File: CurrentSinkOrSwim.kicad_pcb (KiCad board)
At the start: 2 copper layers, 46.5 x 58.2 mm, 23 parts, among them P101 CONN_01X02, P102 CONN_01X03, P103 CONN_01X02, P201 CONN_01X01, Q201 BUK9575, U201 LMV358, U401 LM2931D-R

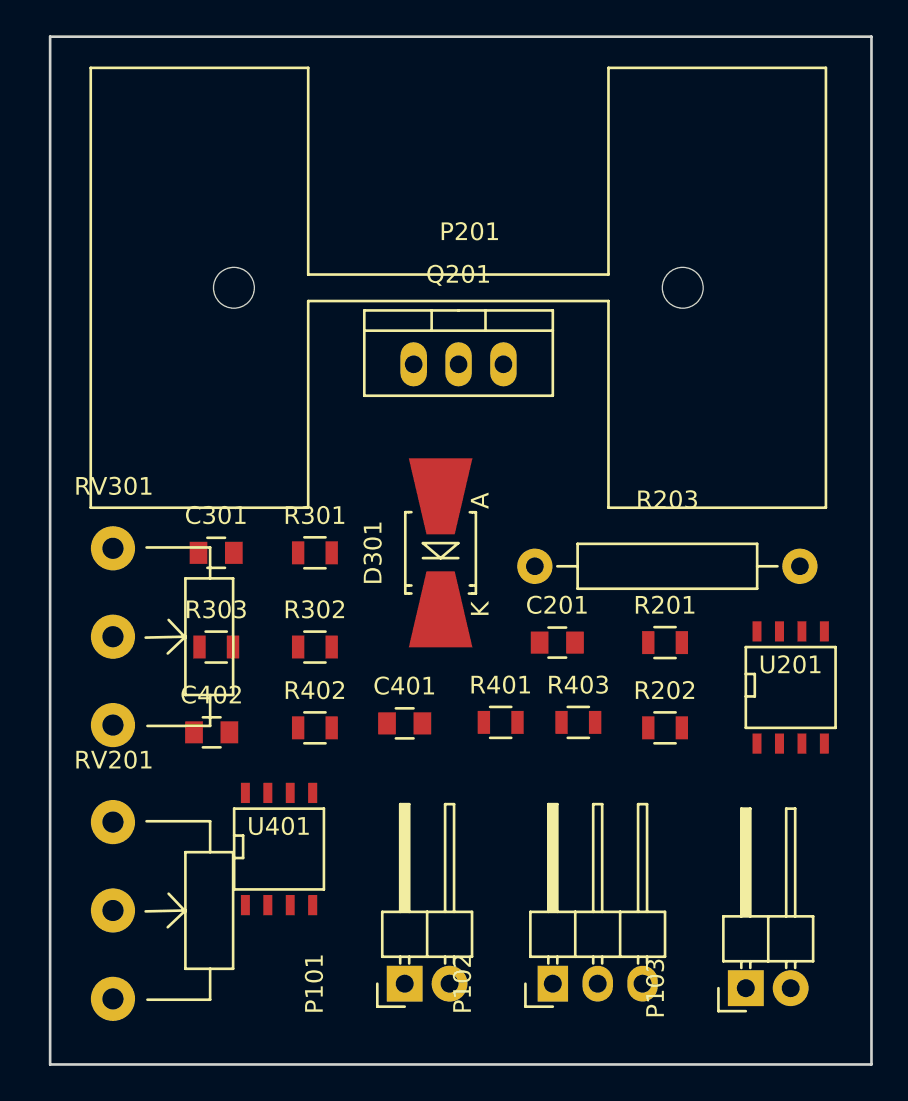
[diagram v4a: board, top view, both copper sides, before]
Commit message: Minor update to layout
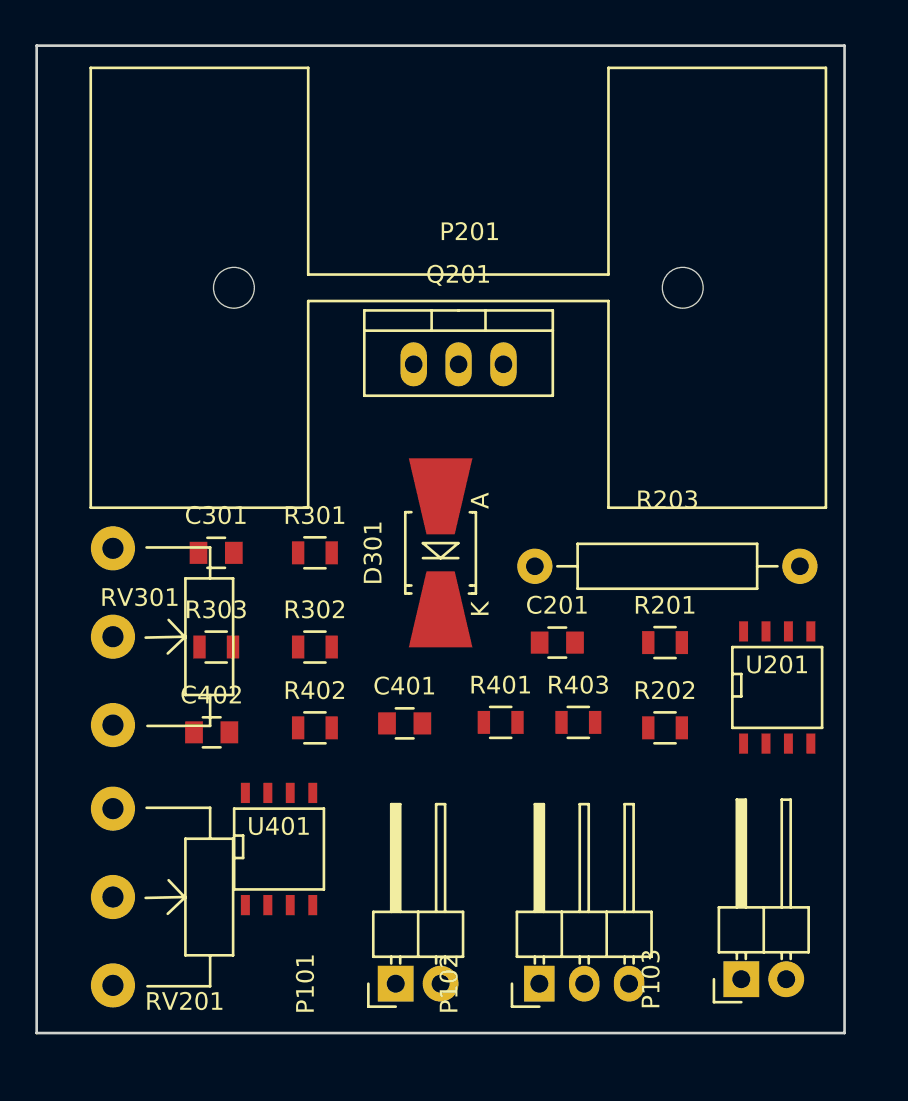
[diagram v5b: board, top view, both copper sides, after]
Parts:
- moved P102 0.76 mm to (130.0, 100.1)
- moved RV201 0.76 mm to (105.9, 90.2)
- moved U201 0.76 mm to (143.5, 83.3)
- moved P103 0.57 mm to (141.5, 99.8)
- moved P101 0.51 mm to (121.9, 100.1)
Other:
- board size 46.5 x 58.2 mm -> 45.7 x 55.9 mm
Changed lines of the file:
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@@
     (links 41)
     (no_connects 41)
-    (area 102.286999 46.406999 148.919001 148.816)
+    (area 101.524999 45.644999 148.919001 102.945001)
     (thickness 1.6)
     (drawings 4)
@@
       (effects (font (size 1 1) (thickness 0.15)))
     )
-    (fp_text value C (at 0 2.1) (layer F.Fab)
+    (fp_text value C (at 2.286 0.762) (layer F.Fab)
       (effects (font (size 1 1) (thickness 0.15)))
     )
@@
   )
   (module Pin_Headers:Pin_Header_Angled_1x02 (layer F.Cu)
-    (at 122.428 100.076 90)
+    (at 121.92 100.076 90)
     (descr "Through hole pin header")
     (tags "pin header")
@@
       (effects (font (size 1 1) (thickness 0.15)))
     )
-    (fp_text value CONN_01X02 (at 0 -3.1 90) (layer F.Fab)
+    (fp_text value CONN_01X02 (at 2.794 -2.54 90) (layer F.Fab)
       (effects (font (size 1 1) (thickness 0.15)))
     )
@@
   )
   (module Pin_Headers:Pin_Header_Angled_1x03 (layer F.Cu)
-    (at 130.81 100.076 90)
+    (at 130.048 100.076 90)
     (descr "Through hole pin header")
     (tags "pin header")
@@
       (effects (font (size 1 1) (thickness 0.15)))
     )
-    (fp_text value CONN_01X03 (at 0 -3.1 90) (layer F.Fab)
+    (fp_text value CONN_01X03 (at 2.794 -2.54 90) (layer F.Fab)
       (effects (font (size 1 1) (thickness 0.15)))
     )
@@
   )
   (module Pin_Headers:Pin_Header_Angled_1x02 (layer F.Cu)
-    (at 141.732 100.33 90)
+    (at 141.478 99.822 90)
     (descr "Through hole pin header")
     (tags "pin header")
@@
       (effects (font (size 1 1) (thickness 0.15)))
     )
-    (fp_text value CONN_01X02 (at 0 -3.1 90) (layer F.Fab)
+    (fp_text value CONN_01X02 (at 2.794 -2.794 90) (layer F.Fab)
       (effects (font (size 1 1) (thickness 0.15)))
     )
@@
       (effects (font (size 1 1) (thickness 0.15)))
     )
-    (fp_text value R (at 0 2.1) (layer F.Fab)
+    (fp_text value R (at 2.286 0.762) (layer F.Fab)
       (effects (font (size 1 1) (thickness 0.15)))
     )
@@
       (effects (font (size 1 1) (thickness 0.15)))
     )
-    (fp_text value .1 (at 7.5 4.0005) (layer F.Fab)
+    (fp_text value .1 (at 7.62 -2.286) (layer F.Fab)
       (effects (font (size 1 1) (thickness 0.15)))
     )
@@
   )
   (module Potentiometers:Potentiometer_WirePads_largePads (layer F.Cu)
-    (at 105.918 90.932)
+    (at 105.918 90.17)
     (descr "Potentiometer, Wire Pads only, RevA, 30 July 2010,")
     (tags "Potentiometer, Wire Pads only, RevA, 30 July 2010,")
-    (fp_text reference RV201 (at 0.0508 -3.49758) (layer F.SilkS)
-      (effects (font (size 1 1) (thickness 0.15)))
-    )
-    (fp_text value POT (at -1.34874 13.25118) (layer F.Fab)
+    (fp_text reference RV201 (at 4.064 10.922) (layer F.SilkS)
+      (effects (font (size 1 1) (thickness 0.15)))
+    )
+    (fp_text value POT (at 7.366 9.906) (layer F.Fab)
       (effects (font (size 1 1) (thickness 0.15)))
     )
@@
     (descr "Potentiometer, Wire Pads only, RevA, 30 July 2010,")
     (tags "Potentiometer, Wire Pads only, RevA, 30 July 2010,")
-    (fp_text reference RV301 (at 0.0508 -3.49758) (layer F.SilkS)
-      (effects (font (size 1 1) (thickness 0.15)))
-    )
-    (fp_text value POT (at -1.34874 13.25118) (layer F.Fab)
+    (fp_text reference RV301 (at 1.524 2.794) (layer F.SilkS)
+      (effects (font (size 1 1) (thickness 0.15)))
+    )
+    (fp_text value POT (at 2.794 12.954) (layer F.Fab)
       (effects (font (size 1 1) (thickness 0.15)))
     )
@@
   )
   (module SMD_Packages:SOIC-8-N (layer F.Cu)
-    (at 144.272 83.312)
+    (at 143.51 83.312)
     (descr "Module Narrow CMS SOJ 8 pins large")
     (tags "CMS SOJ")
@@
     (pad "" np_thru_hole circle (at 12.6873 -0.0127) (size 2.3114 2.3114) (drill 2.3114) (layers *.Cu *.Mask))
   )
-  (gr_line (start 148.844 46.482) (end 102.362 46.482) (angle 90) (layer Edge.Cuts) (width 0.15))
-  (gr_line (start 148.844 104.648) (end 148.844 46.482) (angle 90) (layer Edge.Cuts) (width 0.15))
-  (gr_line (start 102.362 104.648) (end 148.844 104.648) (angle 90) (layer Edge.Cuts) (width 0.15))
-  (gr_line (start 102.362 46.482) (end 102.362 104.648) (angle 90) (layer Edge.Cuts) (width 0.15))
+  (gr_line (start 147.32 46.99) (end 101.6 46.99) (angle 90) (layer Edge.Cuts) (width 0.15))
+  (gr_line (start 147.32 102.87) (end 147.32 46.99) (angle 90) (layer Edge.Cuts) (width 0.15))
+  (gr_line (start 101.6 102.87) (end 147.32 102.87) (angle 90) (layer Edge.Cuts) (width 0.15))
+  (gr_line (start 101.6 46.99) (end 101.6 102.87) (angle 90) (layer Edge.Cuts) (width 0.15))
 )

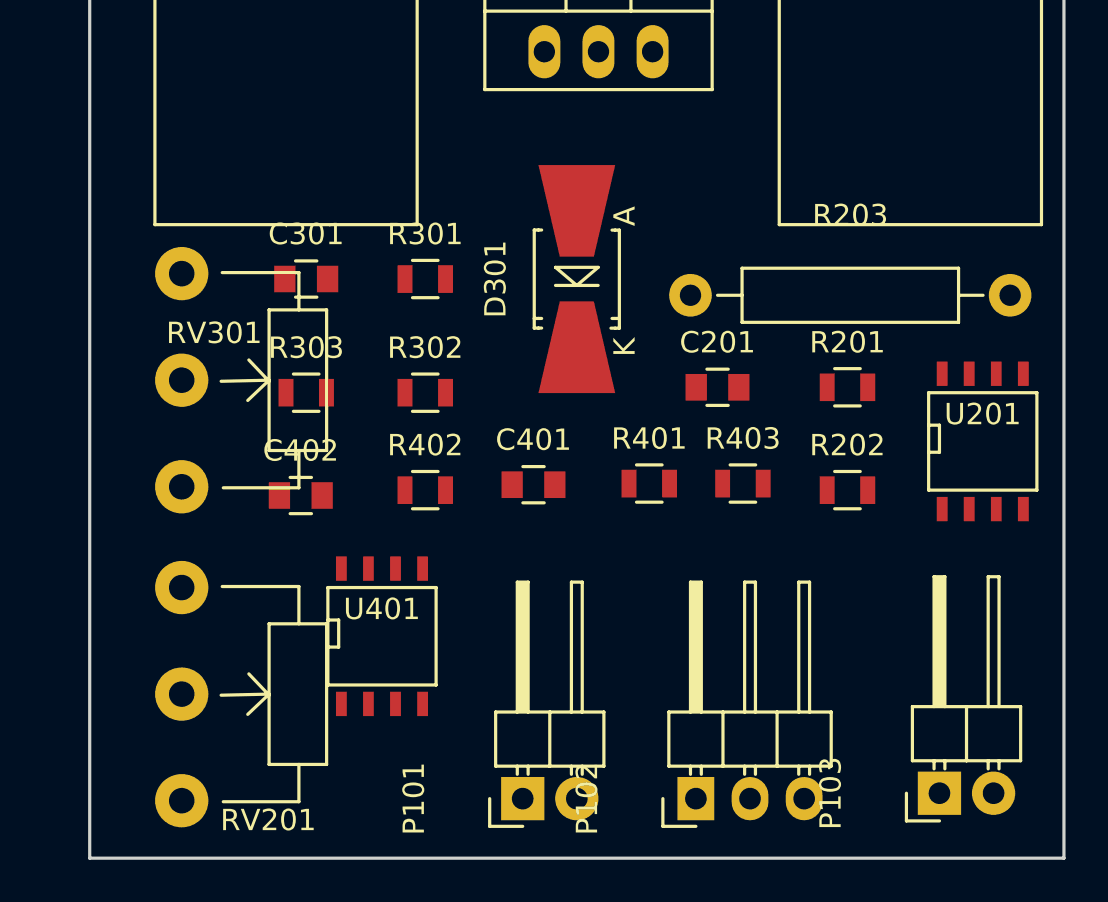
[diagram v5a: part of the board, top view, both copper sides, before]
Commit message: Add potentiometers
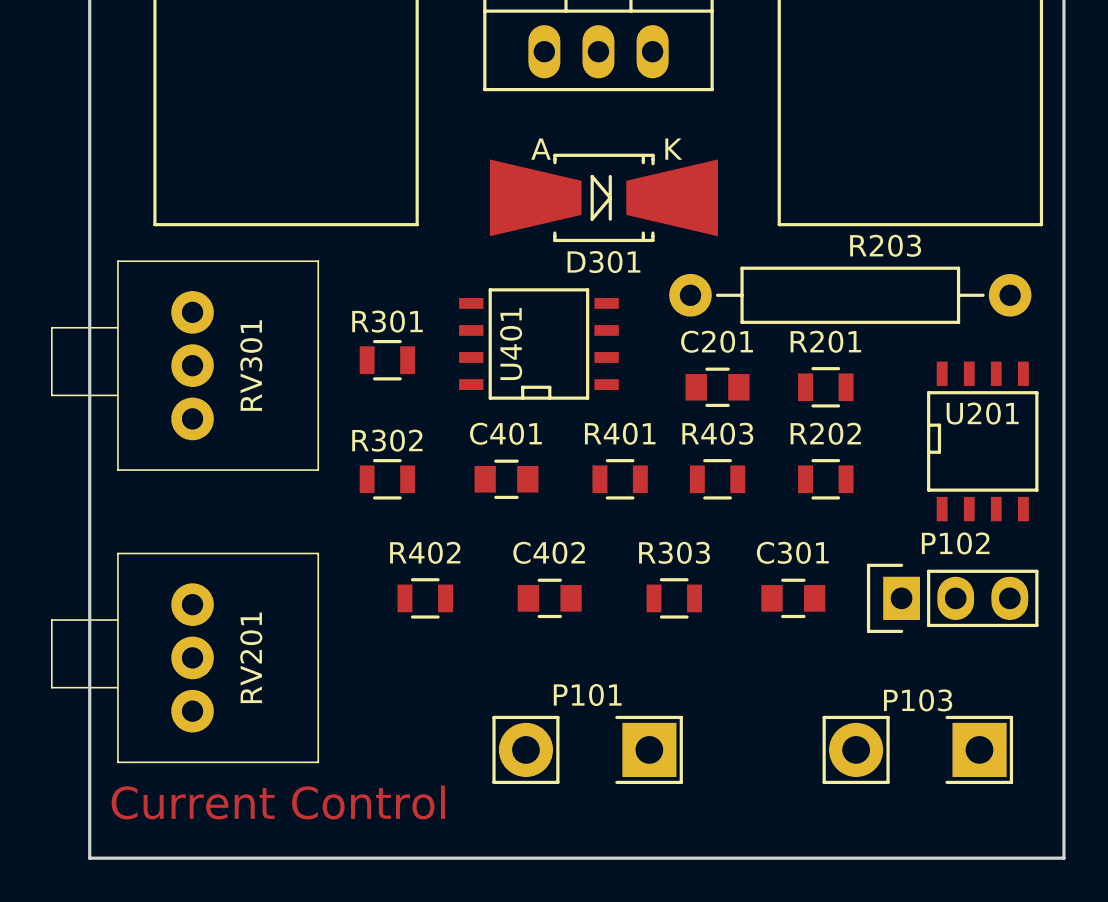
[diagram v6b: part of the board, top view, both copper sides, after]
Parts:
- P101, P103: footprint Pin_Headers:Pin_Header_Angled_1x02 -> current:Terminal_Block_200_mil
- P102: footprint Pin_Headers:Pin_Header_Angled_1x03 -> Pin_Headers:Pin_Header_Straight_1x03
- RV201, RV301: footprint Potentiometers:Potentiometer_WirePads_largePads -> current:P090L-02F25BR10K
- U401: value LM2931D-R -> LM2931
- moved C301 27.3 mm to (134.6, 90.7)
- moved R303 19.8 mm to (129.0, 90.7)
- moved U401 15.6 mm to (122.7, 78.7), turned to 90 degrees
- moved P102 13.5 mm to (139.7, 90.7)
- moved C402 12.6 mm to (123.2, 90.7)
- moved R402 5.08 mm to (117.3, 90.7)
- moved R302 4.44 mm to (115.6, 85.1)
- moved RV301 4.35 mm to (106.4, 79.8), turned to 270 degrees
- moved R301 4.20 mm to (115.6, 79.5)
- moved D301 4.02 mm to (125.7, 71.9), turned to 180 degrees
- moved P101 3.81 mm to (125.0, 97.8), turned to 180 degrees
- moved RV201 3.34 mm to (106.4, 93.5), turned to 270 degrees
- moved P103 2.27 mm to (140.5, 97.8), turned to 180 degrees
- moved R401 1.38 mm to (126.5, 85.1)
- moved C401 1.30 mm to (121.2, 85.1)
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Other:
- board text added: "Current Control"

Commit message: Update layout based on new pot and reisistor values
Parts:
- R201: value R -> 68k
- R301: value R -> 28.7k
- RV201, RV301: value POT -> 10k
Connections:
- R201 pad 1: Net-(R201-Pad1) -> 2.7V
- R201 pad 2: /Current Control/Current_Sink- -> Net-(R201-Pad2)
- R301 pad 1: Net-(R301-Pad1) -> 2.7V
- R301 pad 2: GND -> Net-(R301-Pad2)
- RV201 pad 1: Net-(RV201-Pad1) -> Net-(R201-Pad2)
- RV201 pad 2: 2.7V -> /Current Control/Current_Sink-
- RV201 pad 3: Net-(R201-Pad1) -> Net-(RV201-Pad3)
- RV301 pad 1: Net-(RV301-Pad1) -> Net-(R301-Pad2)
- RV301 pad 2: 2.7V -> GND
- RV301 pad 3: Net-(R301-Pad1) -> Net-(RV301-Pad3)
- U201 pad 3: Net-(R201-Pad1) -> Net-(R201-Pad2)
- U201 pad 5: Net-(R301-Pad1) -> Net-(R301-Pad2)

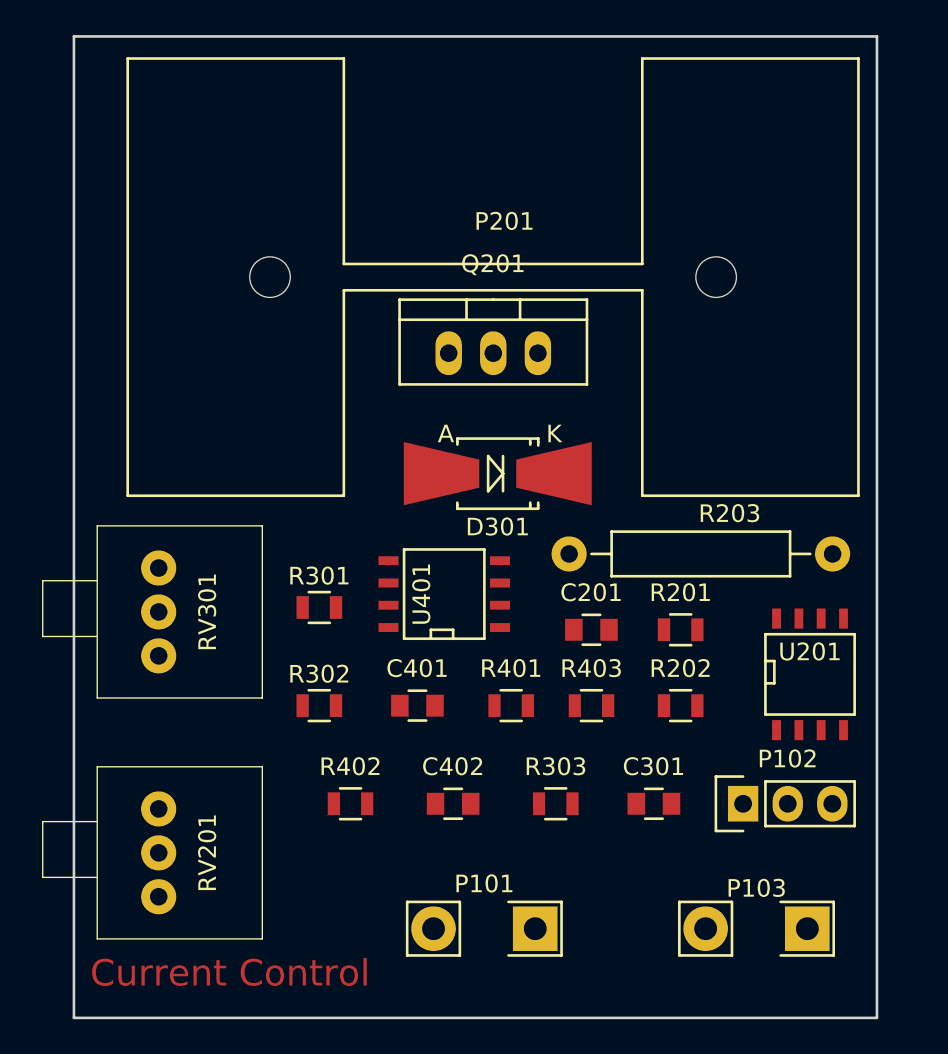
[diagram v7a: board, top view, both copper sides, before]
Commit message: Reorganization of layout, shrink board size, add ground plane
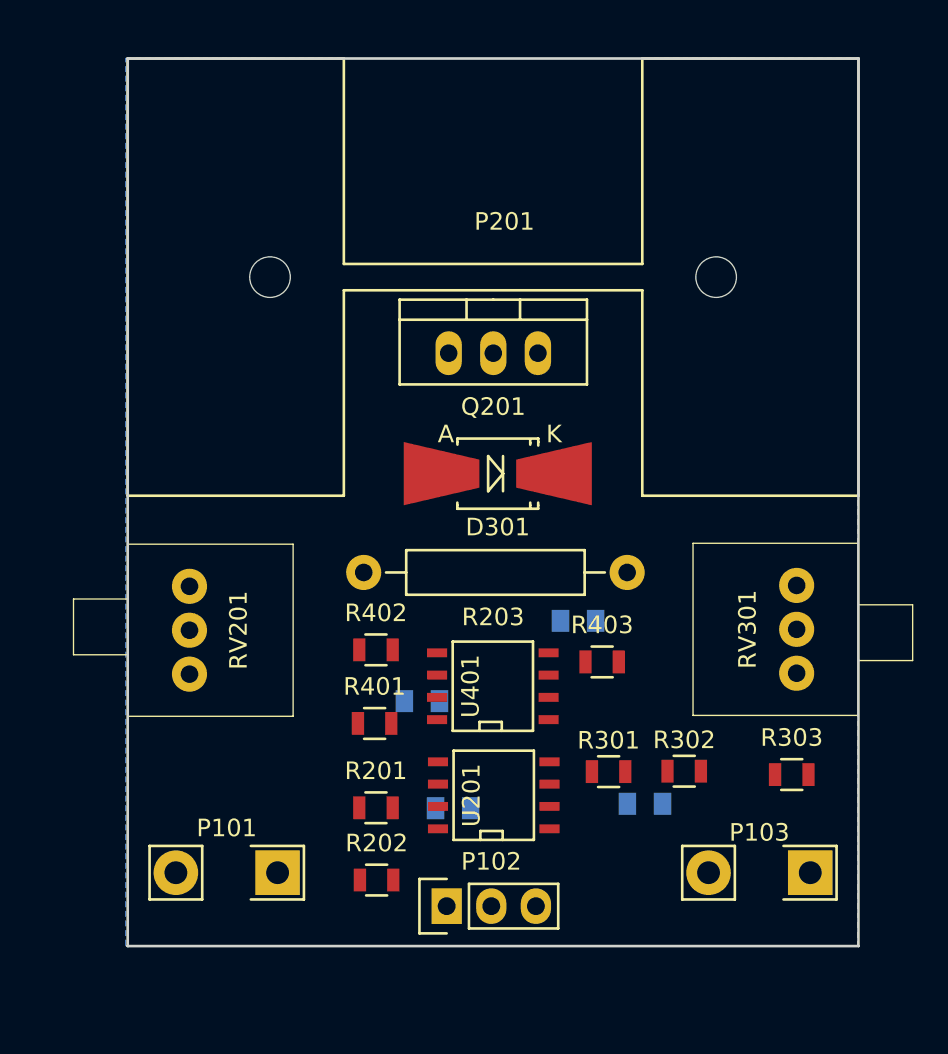
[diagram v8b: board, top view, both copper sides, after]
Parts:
- C201, C301, C401, C402: moved to B.Cu
- moved RV301 36.3 mm to (142.7, 80.7), turned to 90 degrees
- moved R302 21.1 mm to (136.3, 88.8)
- moved R201 20.1 mm to (118.8, 90.9)
- moved R202 20.0 mm to (118.8, 95.0)
- moved U201 19.3 mm to (125.5, 90.2), turned to 90 degrees
- moved R301 18.9 mm to (132.0, 88.8)
- moved P102 17.9 mm to (122.8, 96.5)
- moved P101 15.0 mm to (110.3, 94.6)
- moved R303 13.5 mm to (142.5, 89.0)
- moved RV201 12.8 mm to (108.2, 80.8)
- moved R203 11.7 mm to (118.1, 77.5)
- moved R402 8.88 mm to (118.8, 81.9)
- moved R401 7.84 mm to (118.7, 86.1)
- moved U401 5.93 mm to (125.5, 84.0)
- moved P103 3.19 mm to (140.6, 94.6)
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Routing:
- added copper zone on B.Cu, net GND
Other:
- board size 45.7 x 55.9 mm -> 41.6 x 50.5 mm
- board text removed: "Current Control"
